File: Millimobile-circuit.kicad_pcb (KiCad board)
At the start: 4 copper layers, 15 x 20 mm, 38 parts, among them J1 SM02B-SURS-TF(LF)(SN), J2 DF40C_2.0_-20DS-0.4V_51_, J3 FTSH-105-01-F-DV-P-TR, J4 DF40C_2.0_-20DS-0.4V_51_, M1 Motor_DC, M2 Motor_DC, U1 SN74LVC1G3157YZP, U3 CSD17585F5T, U4 CSD17585F5T, U5 CSD17585F5T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

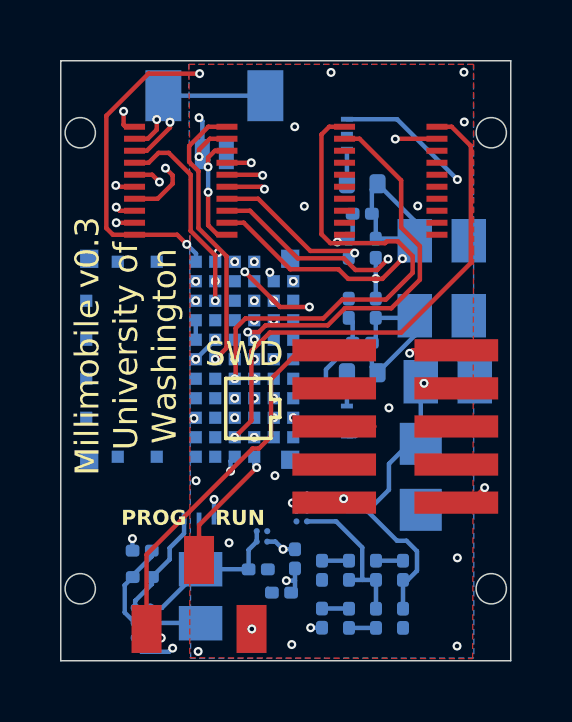
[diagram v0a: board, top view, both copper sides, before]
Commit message: capacitor part change
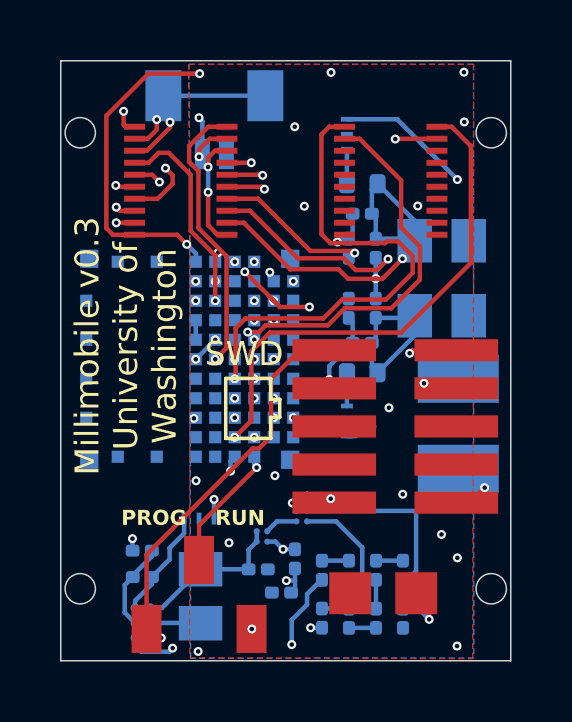
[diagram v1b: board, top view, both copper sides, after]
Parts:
- C1: value 7.5m -> 11m; moved to F.Cu
- C7: value 100u -> 330u; footprint MB-Components:CAPC2012X140N -> MB-Components:CAP_ETPS330MUD
- moved C1 4.08 mm to (110.8, 117.8), turned to 180 degrees
- moved C7 1.44 mm to (113.2, 112.1), turned to 90 degrees
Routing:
- net GND: track 26.5 -> 30.2 mm, vias 20 -> 22
- net SuperCap: track 17.0 -> 15.8 mm, vias 2 -> 3
